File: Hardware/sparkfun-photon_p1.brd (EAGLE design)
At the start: 68.6 x 53.3 mm, 52 parts, among them U1 WM-N-BM-14

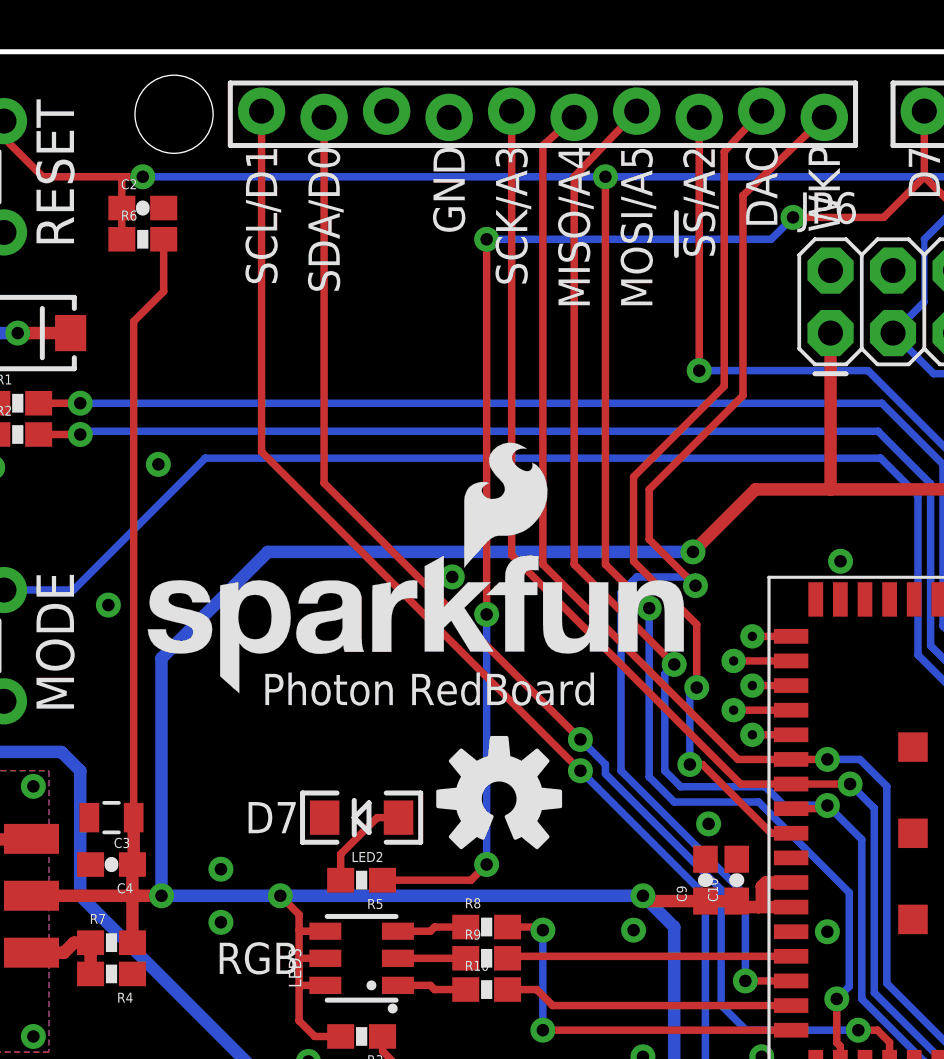
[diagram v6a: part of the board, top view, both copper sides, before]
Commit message: Tweaking some silkscreen
- Changing DAC to "DAC/A6"
- Moving board name silk.
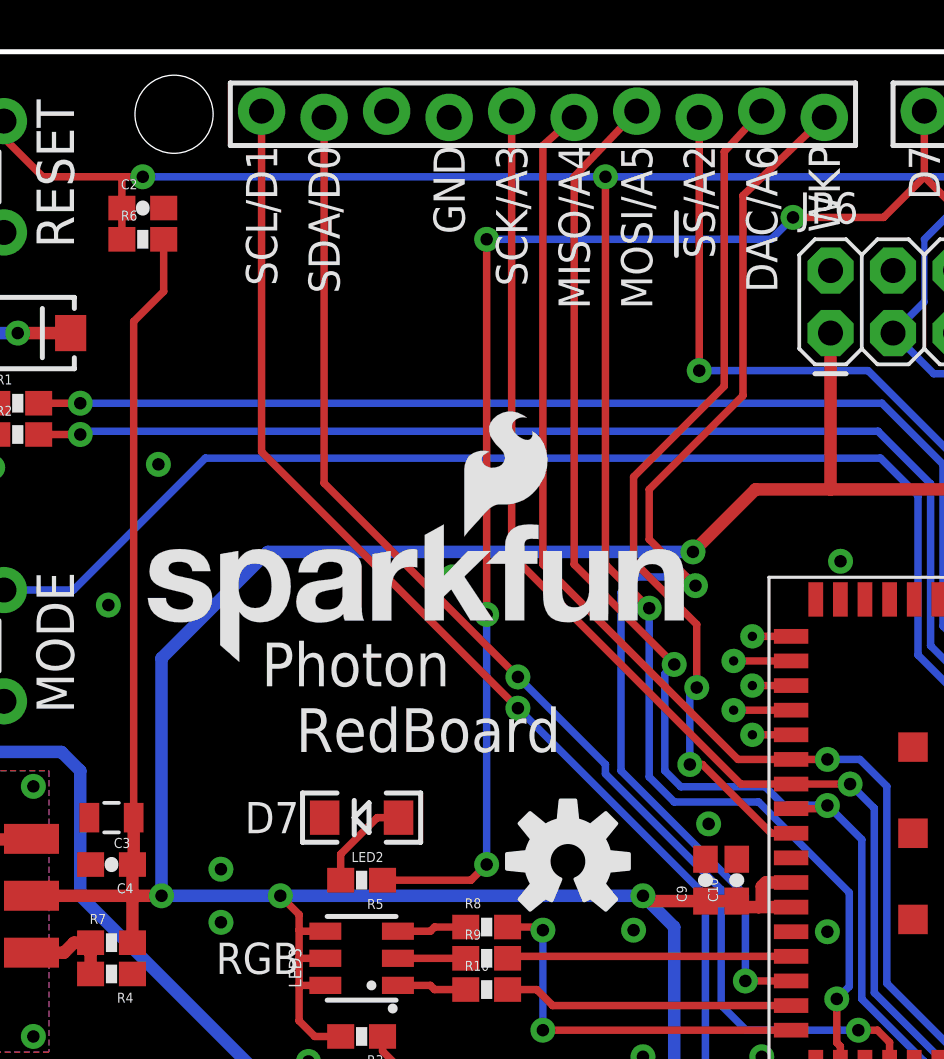
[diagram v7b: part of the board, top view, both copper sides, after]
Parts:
- moved LOGO1 3.78 mm to (31.2, 20.4)
- moved LOGO2 1.27 mm to (13.5, 28.4)
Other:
- board text added: "Based on the Particle Photon, by Particle.io"
- board text added: "DAC/A6"
- board text removed: "Based on the Spark Photon, by Spark.io"
- board text removed: "DAC"
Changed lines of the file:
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@@
 <text x="20.32" y="22.225" size="1.27" layer="21" font="vector" ratio="15" rot="R180" align="center-left">D7</text>
 <text x="20.32" y="10.795" size="1.27" layer="21" font="vector" ratio="15" rot="R180" align="center-left">POWER</text>
-<text x="18.796" y="28.067" size="1.27" layer="21" font="vector" ratio="15" align="top-left">Photon RedBoard</text>
+<text x="18.796" y="29.337" size="1.778" layer="21" font="vector" ratio="15" align="top-left">Photon
+  RedBoard</text>
 <text x="9.652" y="29.337" size="1.524" layer="21" font="vector" ratio="15" rot="R90" align="top-center">MODE</text>
 <text x="9.652" y="48.387" size="1.524" layer="21" font="vector" ratio="15" rot="R90" align="top-center">RESET</text>
@@
 <text x="48.26" y="49.53" size="1.27" layer="21" font="vector" ratio="15" rot="R90" align="center-right">D6</text>
 <text x="45.72" y="49.53" size="1.27" layer="21" font="vector" ratio="15" rot="R90" align="center-right">D7</text>
-<text x="39.116" y="49.53" size="1.27" layer="21" font="vector" ratio="15" rot="R90" align="center-right">DAC</text>
+<text x="39.116" y="49.53" size="1.27" layer="21" font="vector" ratio="15" rot="R90" align="center-right">DAC/A6</text>
 <text x="36.576" y="49.53" size="1.27" layer="21" font="vector" ratio="15" rot="R90" align="center-right">!SS!/A2</text>
 <text x="34.036" y="49.53" size="1.27" layer="21" font="vector" ratio="15" rot="R90" align="center-right">MOSI/A5</text>
@@
 <text x="4.826" y="1.27" size="1.27" layer="21" font="vector" ratio="15" rot="R180" align="center-right">+</text>
 <text x="45.72" y="-11.43" size="1.27" layer="51" font="vector" ratio="15">Jim Lindblom</text>
-<text x="26.67" y="-13.97" size="1.27" layer="51" font="vector" ratio="15">Based on the Spark Photon, by Spark.io</text>
+<text x="26.67" y="-13.97" size="1.27" layer="51" font="vector" ratio="15">Based on the Particle Photon, by Particle.io</text>
 <dimension x1="0" y1="0" x2="13.97" y2="2.54" x3="6.985" y3="-5.08" textsize="1.27" textratio="15" layer="47" dtype="horizontal" unit="inch" precision="3"/>
 <dimension x1="68.58" y1="5.08" x2="0" y2="5.08" x3="34.29" y3="-20.32" textsize="1.27" textratio="15" layer="47" unit="inch" precision="3"/>
@@
 <attribute name="PROD_ID" value="CAP-00810" x="54.61" y="34.29" size="1.778" layer="27" font="vector" ratio="15" display="off"/>
 </element>
-<element name="LOGO2" library="SparkFun-Aesthetics" package="SFE_LOGO_NAME_FLAME_.2" value="SFE_LOGO_NAME_FLAME.2_INCH" x="13.462" y="27.178"/>
-<element name="LOGO1" library="SparkFun-Aesthetics" package="OSHW-LOGO-M" value="OSHW-LOGOM" x="28.448" y="22.987"/>
+<element name="LOGO2" library="SparkFun-Aesthetics" package="SFE_LOGO_NAME_FLAME_.2" value="SFE_LOGO_NAME_FLAME.2_INCH" x="13.462" y="28.448"/>
+<element name="LOGO1" library="SparkFun-Aesthetics" package="OSHW-LOGO-M" value="OSHW-LOGOM" x="31.242" y="20.447"/>
 <element name="U1" library="sparkfun_photon_temp" package="WM-N-BM-14" value="WM-N-BM-14" x="48.26" y="21.59">
 <attribute name="PROD_ID" value="IC-12589" x="48.26" y="21.59" size="1.778" layer="27" font="vector" ratio="15" display="off"/>
@@
 <wire x1="39.37" y1="9.779" x2="36.83" y2="12.319" width="0.3048" layer="16"/>
 <wire x1="36.83" y1="12.319" x2="36.83" y2="19.05" width="0.3048" layer="16"/>
-<via x="31.75" y="24.13" extent="1-16" drill="0.508"/>
-<wire x1="31.75" y1="24.13" x2="18.796" y2="37.084" width="0.3048" layer="1"/>
-<wire x1="36.83" y1="19.05" x2="31.75" y2="24.13" width="0.3048" layer="16"/>
+<via x="29.21" y="26.67" extent="1-16" drill="0.508"/>
+<wire x1="29.21" y1="26.67" x2="18.796" y2="37.084" width="0.3048" layer="1"/>
+<wire x1="36.83" y1="19.05" x2="29.21" y2="26.67" width="0.3048" layer="16"/>
 <wire x1="43.31" y1="12.09" x2="43.31" y2="10.795" width="0.3048" layer="1"/>
 <wire x1="43.31" y1="10.795" x2="43.183" y2="10.668" width="0.3048" layer="1"/>
@@
 <via x="43.04" y="13.589" extent="1-16" drill="0.508"/>
 <wire x1="21.336" y1="50.673" x2="21.336" y2="35.814" width="0.3048" layer="1"/>
-<wire x1="21.336" y1="35.814" x2="31.75" y2="25.4" width="0.3048" layer="1"/>
-<via x="31.75" y="25.4" extent="1-16" drill="0.508"/>
+<wire x1="21.336" y1="35.814" x2="29.21" y2="27.94" width="0.3048" layer="1"/>
+<via x="29.21" y="27.94" extent="1-16" drill="0.508"/>
 <wire x1="37.465" y1="19.304" x2="32.766" y2="24.003" width="0.3048" layer="16"/>
 <wire x1="37.465" y1="14.605" x2="37.465" y2="19.304" width="0.3048" layer="16"/>
 <wire x1="32.766" y1="24.003" x2="32.766" y2="24.384" width="0.3048" layer="16"/>
-<wire x1="32.766" y1="24.384" x2="31.75" y2="25.4" width="0.3048" layer="16"/>
+<wire x1="32.766" y1="24.384" x2="29.21" y2="27.94" width="0.3048" layer="16"/>
 <wire x1="44.31" y1="12.09" x2="44.31" y2="13.094" width="0.3048" layer="1"/>
 <wire x1="44.31" y1="13.094" x2="43.815" y2="13.589" width="0.3048" layer="1"/>

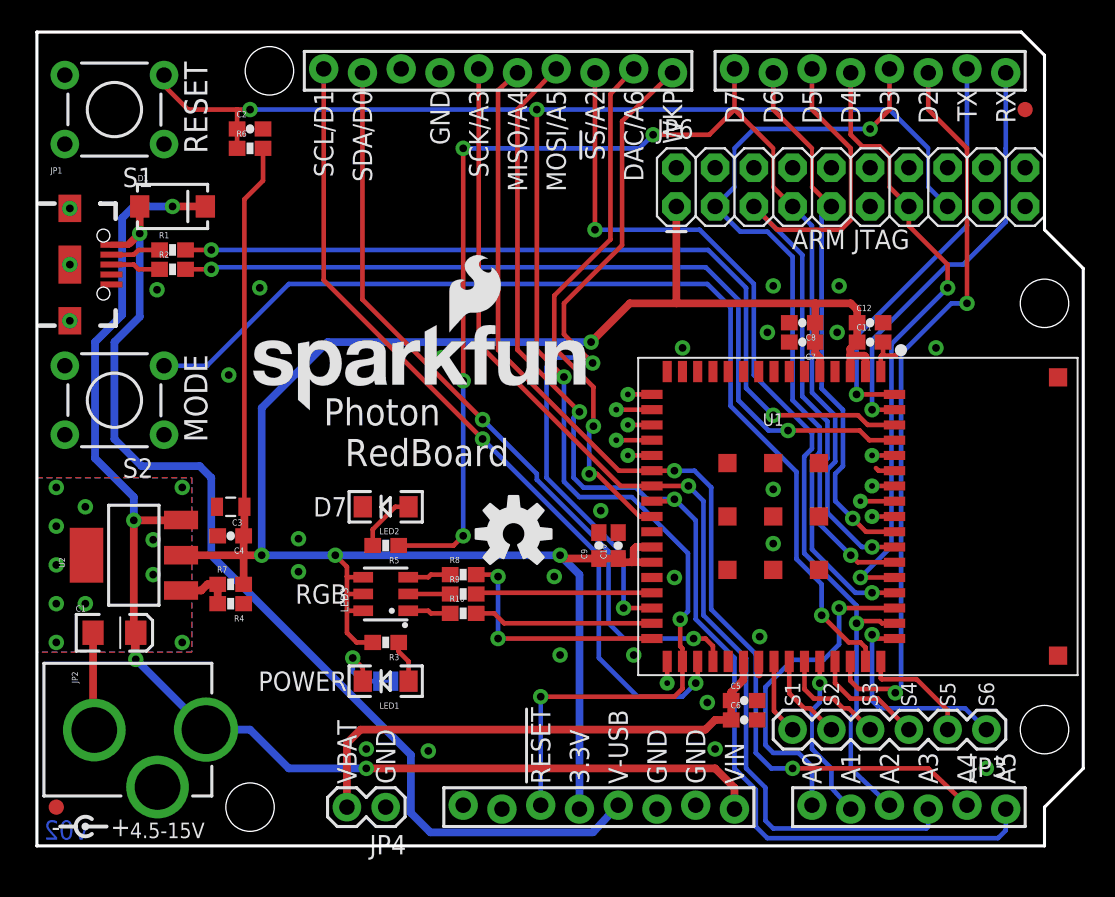
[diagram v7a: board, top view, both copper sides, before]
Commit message: Adding jumper to disconnect D7 LED.
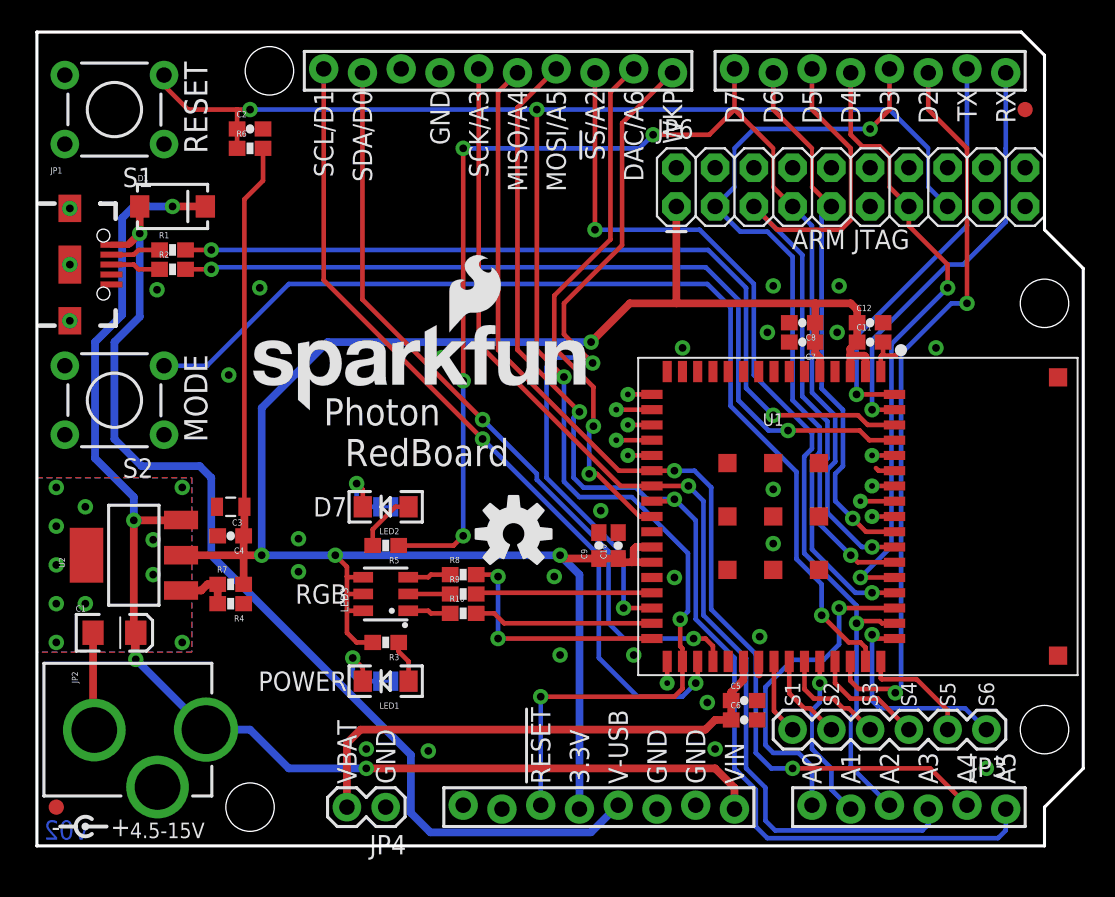
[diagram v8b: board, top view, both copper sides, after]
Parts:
- added SJ2: D7-LED, SparkFun-Passives:PAD-JUMPER-2-NC_BY_TRACE_YES_SILK
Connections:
- new net N$8: LED2.C, SJ2.2
- net GND: now also SJ2.1; no longer LED2.C
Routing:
- net N$8: track 0.00 -> 4.39 mm, vias 0 -> 1
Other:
- board text added: "D7 LED"
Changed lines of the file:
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@@
 <layer number="47" name="Measures" color="7" fill="1" visible="no" active="yes"/>
 <layer number="48" name="Document" color="7" fill="1" visible="no" active="yes"/>
-<layer number="49" name="Reference" color="7" fill="1" visible="no" active="yes"/>
+<layer number="49" name="Reference" color="7" fill="1" visible="yes" active="yes"/>
 <layer number="50" name="dxf" color="7" fill="1" visible="no" active="no"/>
 <layer number="51" name="tDocu" color="6" fill="1" visible="yes" active="yes"/>
@@
 <text x="24.003" y="10.795" size="0.8128" layer="22" font="vector" ratio="15" rot="MR0" align="center-right">PWR
 LED</text>
+<text x="24.003" y="22.225" size="0.8128" layer="22" font="vector" ratio="15" rot="MR0" align="center-right">D7
+LED</text>
 </plain>
 <attributes>
@@
 <element name="TP10" library="SparkFun-Passives" package="TP_15TH" value="TEST-POINTTP_15TH_THRU" x="41.31" y="10.668"/>
 <element name="SJ1" library="SparkFun-Passives" package="PAD-JUMPER-2-NC_BY_TRACE_YES_SILK" value="PWR-LED" x="22.86" y="10.795" rot="MR0"/>
+<element name="SJ2" library="SparkFun-Passives" package="PAD-JUMPER-2-NC_BY_TRACE_YES_SILK" value="D7-LED" x="22.86" y="22.225" rot="MR0"/>
 </elements>
 <signals>
@@
 <contactref element="C2" pad="2"/>
 <contactref element="S2" pad="1"/>
-<contactref element="LED2" pad="C"/>
 <polygon width="0.254" layer="16" isolate="0.3048" rank="6">
 <vertex x="0" y="0"/>
@@
 <via x="12.573" y="30.861" extent="1-16" drill="0.508"/>
 <contactref element="SJ1" pad="1"/>
+<contactref element="SJ2" pad="1"/>
 </signal>
 <signal name="3.3V">
@@
 <wire x1="6.096" y1="39.497" x2="6.74" y2="40.141" width="0.508" layer="1"/>
 <via x="6.74" y="40.141" extent="1-16" drill="0.508"/>
-<wire x1="38.1" y1="2.667" x2="36.449" y2="0.889" width="0.508" layer="16"/>
-<wire x1="36.449" y1="0.889" x2="25.781" y2="0.889" width="0.508" layer="16"/>
+<wire x1="38.1" y1="2.667" x2="36.322" y2="0.889" width="0.508" layer="16"/>
+<wire x1="36.322" y1="0.889" x2="25.781" y2="0.889" width="0.508" layer="16"/>
 <wire x1="6.74" y1="41.91" x2="6.74" y2="40.141" width="0.508" layer="1"/>
 <wire x1="6.858" y1="24.892" x2="10.668" y2="24.892" width="0.508" layer="16"/>
@@
 <via x="36.195" y="24.384" extent="1-16" drill="0.508"/>
 <via x="36.4744" y="27.5082" extent="1-16" drill="0.508"/>
-<wire x1="37.592" y1="49.276" x2="39.116" y2="50.927" width="0.3048" layer="1"/>
-<wire x1="37.592" y1="39.751" x2="37.592" y2="49.276" width="0.3048" layer="1"/>
+<wire x1="37.592" y1="49.403" x2="39.116" y2="50.927" width="0.3048" layer="1"/>
+<wire x1="37.592" y1="39.751" x2="37.592" y2="49.403" width="0.3048" layer="1"/>
 <wire x1="37.592" y1="39.751" x2="33.909" y2="36.068" width="0.3048" layer="1"/>
 <wire x1="33.909" y1="36.068" x2="33.909" y2="32.639" width="0.3048" layer="1"/>
@@
 <wire x1="62.992" y1="0.508" x2="63.5" y2="1.016" width="0.3048" layer="16"/>
 <wire x1="63.5" y1="1.016" x2="63.5" y2="2.413" width="0.3048" layer="16"/>
-<wire x1="31.496" y1="32.512" x2="31.496" y2="48.26" width="0.3048" layer="1"/>
-<wire x1="31.496" y1="48.26" x2="34.036" y2="50.927" width="0.3048" layer="1"/>
+<wire x1="31.496" y1="32.512" x2="31.496" y2="48.387" width="0.3048" layer="1"/>
+<wire x1="31.496" y1="48.387" x2="34.036" y2="50.927" width="0.3048" layer="1"/>
 <wire x1="40.31" y1="22.59" x2="41.656" y2="22.59" width="0.3048" layer="1"/>
 <wire x1="41.656" y1="22.59" x2="41.783" y2="22.717" width="0.3048" layer="1"/>
@@
 <wire x1="28.956" y1="50.927" x2="28.956" y2="32.893" width="0.3048" layer="1"/>
 <wire x1="28.956" y1="32.893" x2="38.259" y2="23.59" width="0.3048" layer="1"/>
-<wire x1="47.752" y1="1.651" x2="48.26" y2="1.143" width="0.3048" layer="16"/>
-<wire x1="48.26" y1="1.143" x2="58.293" y2="1.143" width="0.3048" layer="16"/>
-<wire x1="58.293" y1="1.143" x2="58.42" y2="1.27" width="0.3048" layer="16"/>
-<wire x1="58.42" y1="1.27" x2="58.42" y2="2.413" width="0.3048" layer="16"/>
+<wire x1="47.752" y1="1.651" x2="48.387" y2="1.016" width="0.3048" layer="16"/>
+<wire x1="48.387" y1="1.016" x2="58.039" y2="1.016" width="0.3048" layer="16"/>
+<wire x1="58.039" y1="1.016" x2="58.42" y2="1.397" width="0.3048" layer="16"/>
+<wire x1="58.42" y1="1.397" x2="58.42" y2="2.413" width="0.3048" layer="16"/>
 <wire x1="43.688" y1="15.113" x2="43.688" y2="22.606" width="0.3048" layer="16"/>
 <wire x1="43.688" y1="22.606" x2="42.704" y2="23.59" width="0.3048" layer="16"/>
@@
 <wire x1="47.117" y1="12.573" x2="47.117" y2="6.096" width="0.3048" layer="16"/>
 <via x="49.53" y="5.08" extent="1-16" drill="0.508"/>
-<wire x1="49.53" y1="5.08" x2="58.42" y2="5.08" width="0.3048" layer="1"/>
-<wire x1="58.42" y1="5.08" x2="60.96" y2="2.667" width="0.3048" layer="1"/>
-<wire x1="30.226" y1="32.512" x2="30.226" y2="49.53" width="0.3048" layer="1"/>
-<wire x1="30.226" y1="49.53" x2="31.496" y2="50.673" width="0.3048" layer="1"/>
+<wire x1="49.53" y1="5.08" x2="58.547" y2="5.08" width="0.3048" layer="1"/>
+<wire x1="58.547" y1="5.08" x2="60.96" y2="2.667" width="0.3048" layer="1"/>
+<wire x1="30.226" y1="32.512" x2="30.226" y2="49.403" width="0.3048" layer="1"/>
+<wire x1="30.226" y1="49.403" x2="31.496" y2="50.673" width="0.3048" layer="1"/>
 <wire x1="44.196" y1="15.494" x2="44.196" y2="23.495" width="0.3048" layer="16"/>
 <wire x1="49.53" y1="5.08" x2="48.133" y2="5.08" width="0.3048" layer="16"/>
@@
 <wire x1="50.8" y1="26.035" x2="50.292" y2="25.527" width="0.3048" layer="16"/>
 <wire x1="50.292" y1="25.527" x2="50.292" y2="19.177" width="0.3048" layer="16"/>
-<wire x1="55.88" y1="2.667" x2="53.34" y2="5.08" width="0.3048" layer="16"/>
-<wire x1="53.34" y1="5.08" x2="53.34" y2="6.858" width="0.3048" layer="16"/>
+<wire x1="55.88" y1="2.667" x2="53.34" y2="5.207" width="0.3048" layer="16"/>
+<wire x1="53.34" y1="5.207" x2="53.34" y2="6.858" width="0.3048" layer="16"/>
 <wire x1="56.21" y1="14.59" x2="55.387" y2="14.59" width="0.3048" layer="1"/>
 <wire x1="55.387" y1="14.59" x2="55.245" y2="14.732" width="0.3048" layer="1"/>
@@
 <via x="51.31" y="10.666" extent="1-16" drill="0.508"/>
 <wire x1="51.31" y1="10.666" x2="51.31" y2="9.4" width="0.3048" layer="16"/>
-<wire x1="52.07" y1="3.81" x2="53.34" y2="2.413" width="0.3048" layer="16"/>
+<wire x1="52.07" y1="3.683" x2="53.34" y2="2.413" width="0.3048" layer="16"/>
 <wire x1="51.31" y1="9.4" x2="50.8" y2="8.89" width="0.3048" layer="16"/>
 <wire x1="50.8" y1="8.89" x2="50.8" y2="8.382" width="0.3048" layer="16"/>
@@
 <wire x1="50.8" y1="6.858" x2="50.8" y2="6.35" width="0.3048" layer="16"/>
 <wire x1="50.8" y1="6.35" x2="52.07" y2="5.08" width="0.3048" layer="16"/>
-<wire x1="52.07" y1="5.08" x2="52.07" y2="3.81" width="0.3048" layer="16"/>
+<wire x1="52.07" y1="5.08" x2="52.07" y2="3.683" width="0.3048" layer="16"/>
 </signal>
 <signal name="A0">
@@
 <wire x1="33.401" y1="24.13" x2="33.401" y2="31.369" width="0.3048" layer="16"/>
 <via x="36.4236" y="31.6484" extent="1-16" drill="0.508"/>
-<wire x1="38.354" y1="47.498" x2="41.656" y2="50.673" width="0.3048" layer="1"/>
-<wire x1="38.354" y1="39.37" x2="38.354" y2="47.498" width="0.3048" layer="1"/>
+<wire x1="38.354" y1="47.371" x2="41.656" y2="50.673" width="0.3048" layer="1"/>
+<wire x1="38.354" y1="39.37" x2="38.354" y2="47.371" width="0.3048" layer="1"/>
 <wire x1="34.544" y1="35.56" x2="38.354" y2="39.37" width="0.3048" layer="1"/>
 <wire x1="34.036" y1="32.004" x2="33.401" y2="31.369" width="0.3048" layer="16"/>
@@
 <wire x1="21.36" y1="11.66" x2="20.701" y2="12.319" width="0.3048" layer="1"/>
 <via x="20.701" y="12.319" extent="1-16" drill="0.508"/>
-<wire x1="20.701" y1="12.319" x2="20.701" y2="11.43" width="0.3048" layer="16"/>
-<wire x1="20.701" y1="11.43" x2="21.336" y2="10.795" width="0.3048" layer="16"/>
-<wire x1="21.336" y1="10.795" x2="22.352" y2="10.795" width="0.3048" layer="16"/>
+<wire x1="20.701" y1="12.319" x2="20.701" y2="11.176" width="0.3048" layer="16"/>
+<wire x1="20.701" y1="11.176" x2="21.082" y2="10.795" width="0.3048" layer="16"/>
+<wire x1="21.082" y1="10.795" x2="22.352" y2="10.795" width="0.3048" layer="16"/>
+</signal>
+<signal name="N$8">
+<contactref element="SJ2" pad="2"/>
+<contactref element="LED2" pad="C"/>
+<wire x1="21.36" y1="22.225" x2="21.36" y2="23.344" width="0.3048" layer="1"/>
+<wire x1="21.36" y1="23.344" x2="20.955" y2="23.749" width="0.3048" layer="1"/>
+<via x="20.955" y="23.749" extent="1-16" drill="0.508"/>
+<wire x1="20.955" y1="23.749" x2="20.955" y2="22.606" width="0.3048" layer="16"/>
+<wire x1="20.955" y1="22.606" x2="21.336" y2="22.225" width="0.3048" layer="16"/>
+<wire x1="21.336" y1="22.225" x2="22.352" y2="22.225" width="0.3048" layer="16"/>
 </signal>
 </signals>
